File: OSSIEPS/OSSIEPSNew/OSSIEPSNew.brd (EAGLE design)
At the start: 94 x 88 mm, 99 parts, among them U1 LT3479, U11 SN74LVC1T45-EP, U13 MAX890L, U14 MAX890L, U2 MAX4376, U3 LT3652, U4 LTC4411, U5 LTC4411, U6 LTC4425, U8 LTC4411, X1 ESQ-126-38-G-D, X2 53015-03, X3 5268-02, X4 5268-02, X5 5268-03, X6 5268-02, X8 E62-10K

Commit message: eps board almost done
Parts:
- moved R17 3.01 mm to (17.8, 19.7), turned to 180 degrees
- moved R25 2.02 mm to (17.8, 16.7), turned to 0 degrees
- moved C6 1.27 mm to (24.4, 31.9)
- moved C1 1.27 mm to (16.2, 25.1)
- moved C2 1.27 mm to (21.0, 36.5)
- moved C5 1.27 mm to (25.4, 29.2)
- moved C7 1.27 mm to (25.6, 34.3)
- moved C8 1.27 mm to (23.2, 35.6)
- moved C9 1.27 mm to (21.9, 26.4)
- moved D1 1.27 mm to (16.2, 38.4)
- moved JP7 1.27 mm to (6.35, 44.1)
- moved L2 1.27 mm to (9.53, 34.3)
- moved R1 1.27 mm to (15.6, 27.0)
- moved R2 1.27 mm to (26.0, 31.3)
- moved R3 1.27 mm to (25.4, 27.6)
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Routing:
- net 3.3VOBC: track 5.14 -> 174.9 mm, vias 0 -> 4
- net VBUS: track 70.8 -> 230.2 mm, vias 2 -> 8
- net VSUPERCAP: track 51.7 -> 147.8 mm, vias 2 -> 4
- net SCCHG_EN: track 9.86 -> 105.1 mm, vias 0 -> 4
- net SCOUT_EN: track 13.2 -> 93.8 mm, vias 0 -> 4
- net SC_-PFO: track 10.7 -> 80.8 mm, vias 2 -> 4
- net SC_-ON: track 3.42 -> 70.8 mm, vias 0 -> 3
- net BAT_-CHRG: track 10.7 -> 77.3 mm, vias 0 -> 3
- net BAT_-FAULT: track 7.09 -> 72.8 mm, vias 0 -> 1
- net VBAT: track 125.8 -> 186.2 mm, vias 3 -> 5
- net SOLAR_-ON: track 33.1 -> 69.4 mm, vias 0 -> 2
- net VSC_IN: track 0.00 -> 20.5 mm
- net BAT_-ON: track 3.26 -> 20.8 mm
- net GND: track 32.8 -> 40.1 mm, vias 66 -> 70
- net N$46: track 68.7 -> 65.9 mm
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
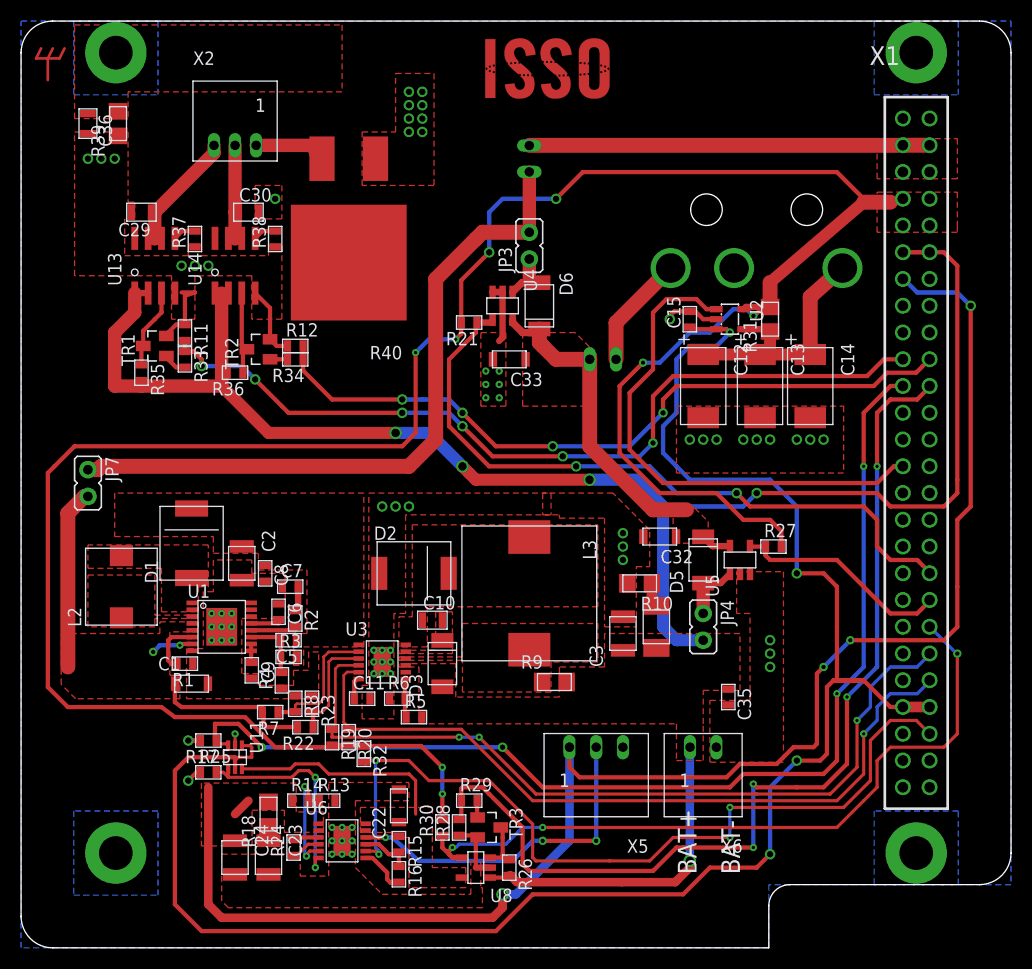
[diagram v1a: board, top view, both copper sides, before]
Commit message: battery supercap board added / library added
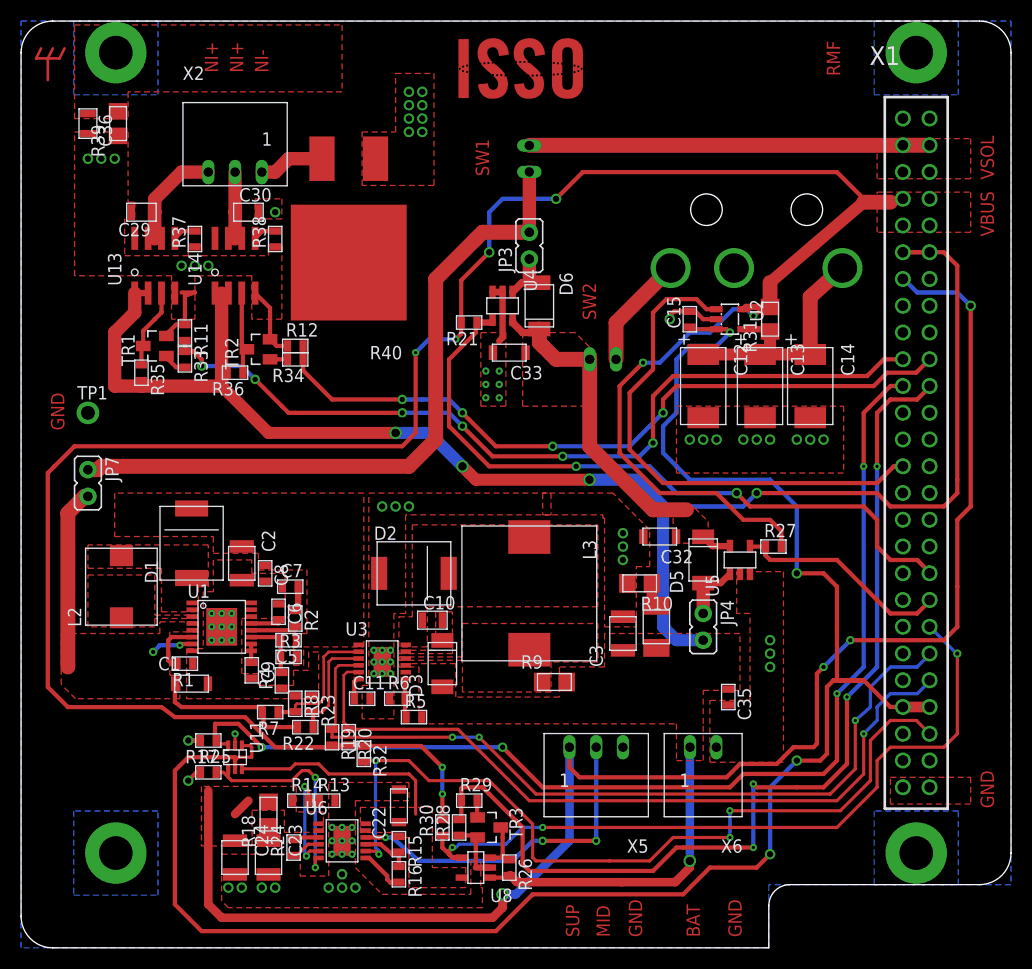
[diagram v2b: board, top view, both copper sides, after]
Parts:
- added TP1: TP, OSSI:TP-13
- X2: value 53015-03 -> 5268-03; device OSSI:53015-03 -> OSSI:5268-03
- moved X2 2.54 mm to (20.3, 73.7)
- moved U$1 2.54 mm to (53.3, 86.4)
- moved C33 0.63 mm to (46.4, 56.5)
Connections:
- net GND: now also TP1.TP
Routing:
- net ANT_COIL2: track 10.5 -> 7.99 mm
- net ANT_COIL1: track 13.3 -> 12.0 mm
- net N$57: track 7.15 -> 6.24 mm
- net N$20: track 20.8 -> 21.5 mm
- net GND: vias 70 -> 78
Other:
- board text added: "BAT"
- board text added: "GND"
- board text added: "MID"
- board text added: "NI+"
- board text added: "NI-"
- board text added: "RMF"
- board text added: "SUP"
- board text added: "SW1"
- board text added: "SW2"
- board text added: "VBUS"
- board text added: "VSOL"
- board text removed: "BAT+"
- board text removed: "BAT-"

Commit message: beta 1 release
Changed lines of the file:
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@@
 <setting verticaltext="up"/>
 </settings>
-<grid distance="1" unitdist="mm" unit="mm" style="lines" multiple="1" display="yes" altdistance="0.0125" altunitdist="inch" altunit="inch"/>
+<grid distance="1.27" unitdist="mm" unit="mm" style="lines" multiple="1" display="yes" altdistance="0.0125" altunitdist="inch" altunit="inch"/>
 <layers>
 <layer number="1" name="Top" color="4" fill="1" visible="yes" active="yes"/>
@@
 <layer number="27" name="tValues" color="7" fill="1" visible="no" active="yes"/>
 <layer number="28" name="bValues" color="7" fill="1" visible="no" active="yes"/>
-<layer number="29" name="tStop" color="7" fill="3" visible="no" active="yes"/>
+<layer number="29" name="tStop" color="7" fill="3" visible="yes" active="yes"/>
 <layer number="30" name="bStop" color="7" fill="6" visible="no" active="yes"/>
 <layer number="31" name="tCream" color="7" fill="4" visible="no" active="yes"/>
@@
 <text x="54.5934875" y="59.608721875" size="1.27" layer="29" font="vector" rot="SR90">SW2</text>
 <text x="44.4334875" y="73.261221875" size="1.27" layer="29" font="vector" rot="SR90">SW1</text>
-<text x="92.3759875" y="72.943721875" size="1.27" layer="1" font="vector" rot="SR90">VSOL</text>
-<text x="92.3759875" y="67.546221875" size="1.27" layer="1" font="vector" rot="SR90">VBUS</text>
-<text x="92.3759875" y="67.546221875" size="1.27" layer="29" font="vector" rot="SR90">VBUS</text>
-<text x="92.3759875" y="72.943721875" size="1.27" layer="29" font="vector" rot="SR90">VSOL</text>
-<text x="92.3759875" y="13.253721875" size="1.27" layer="1" font="vector" rot="SR90">GND</text>
-<text x="92.3759875" y="13.253721875" size="1.27" layer="29" font="vector" rot="SR90">GND</text>
+<text x="92.3759875" y="78.341221875" size="1.27" layer="1" font="vector" rot="SR90">VSOL</text>
+<text x="92.3759875" y="62.466221875" size="1.27" layer="1" font="vector" rot="SR90">VBUS</text>
+<text x="92.3759875" y="62.466221875" size="1.27" layer="29" font="vector" rot="SR90">VBUS</text>
+<text x="92.3759875" y="78.341221875" size="1.27" layer="29" font="vector" rot="SR90">VSOL</text>
+<text x="92.3759875" y="18.333721875" size="1.27" layer="1" font="vector" rot="SR90">GND</text>
+<text x="92.3759875" y="18.333721875" size="1.27" layer="29" font="vector" rot="SR90">GND</text>
 <text x="4.1109875" y="49.131221875" size="1.27" layer="29" font="vector" rot="SR90">GND</text>
 <text x="4.1109875" y="49.131221875" size="1.27" layer="1" font="vector" rot="SR90">GND</text>
@@
 <polygon width="0.3048" layer="1" thermals="no">
 <vertex x="82.55" y="16.1925"/>
-<vertex x="90.17" y="16.1925"/>
-<vertex x="90.17" y="13.6525"/>
+<vertex x="92.71" y="16.1925"/>
+<vertex x="92.71" y="13.6525"/>
 <vertex x="82.55" y="13.6525"/>
 </polygon>
@@
 <polygon width="0.3048" layer="1" thermals="no">
 <vertex x="81.28" y="71.755"/>
-<vertex x="90.17" y="71.755"/>
-<vertex x="90.17" y="67.945"/>
+<vertex x="92.71" y="71.755"/>
+<vertex x="92.71" y="67.945"/>
 <vertex x="81.28" y="67.945"/>
 </polygon>
@@
 <polygon width="0.3048" layer="1" thermals="no">
 <vertex x="81.28" y="76.835"/>
-<vertex x="90.17" y="76.835"/>
-<vertex x="90.17" y="73.025"/>
+<vertex x="92.71" y="76.835"/>
+<vertex x="92.71" y="73.025"/>
 <vertex x="81.28" y="73.025"/>
 </polygon>

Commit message: schematics renumbered
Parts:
- removed C29, C30: 100nF, 0805, OSSI:C0805(2012)
- removed C32, C33: 4.7uF, 1206, OSSI:C1206-GCM31
- removed C35: (no value), OSSI:C0603(1608)
- removed C36: (no value), OSSI:C0805(2012)
- removed D6: PMEG6020EP, OSSI:PMEG6020EP
- removed L3: 10uH, OSSI:RLF12545
- removed U11: SN74LVC1T45-EP, OSSI:SOT-6DCK
- removed U13, U14: MAX890L, OSSI:SO8
- removed X8: E62-10K, OSSI:E62-10K
- added C16: 100uF, OSSI:C1210-TMK325
- added C17, C21: 10uF, OSSI:C1210-GCM32
- added C18: 10nF, OSSI:C0603(1608)
- added C19: 470pF, OSSI:C0603(1608)
- added C20: 0.1uF, OSSI:C0603(1608)
- added D4: PMEG6020EP, OSSI:PMEG6020EP
- added L1: 4.7uH, OSSI:RLF7030
- added U10, U7: LTC4411, OSSI:TSOT23-5
- added U9: MAX4376, OSSI:SOT23-5DBV
- added X7: 5268-02, OSSI:5628-02
- C1: value 2.2uF -> (none); device OSSI:C1206-GCM31 -> OSSI:C0805(2012)
- C10: value 1uF, 100V -> 0 Ohm; device OSSI:C0805(2012) -> OSSI:C0603(1608)
- C11: value 0 Ohm -> (none)
- C2, C3: value 10uF -> 100nF, 0805; device OSSI:C1210-GCM32 -> OSSI:C0805(2012)
- C22: value 2.2uF -> 1uF, 100V; device OSSI:C1206-GCM31 -> OSSI:C0805(2012)
- C23: value 22uF -> 0.1uF; device OSSI:C1210-GCM32 -> OSSI:C0603(1608)
- C24: value 22uF -> 4.7uF, 1206; device OSSI:C1210-GCM32 -> OSSI:C1206-GCM31
- C4: value 100uF -> 2.2uF; device OSSI:C1210-TMK325 -> OSSI:C1206-GCM31
- C5: value 470pF -> 22uF; device OSSI:C0603(1608) -> OSSI:C1210-GCM32
- C6: value 0.1uF -> 22uF; device OSSI:C0603(1608) -> OSSI:C1210-GCM32
- C7: value 10nF -> 100pF
- C8: value 0.1uF -> 2.2uF; device OSSI:C0603(1608) -> OSSI:C1206-GCM31
- C9: value 100pF -> 4.7uF, 1206; device OSSI:C0603(1608) -> OSSI:C1206-GCM31
- D1: value STPS5L60 -> PMEG6020EP; device OSSI:STPS5L60 -> OSSI:PMEG6020EP
- D3: value PMEG6020EP -> STPS5L60; device OSSI:PMEG6020EP -> OSSI:STPS5L60
- L2: value 4.7uH -> 10uH; device OSSI:RLF7030 -> OSSI:RLF12545
- R1: value 17.8k -> 511; device OSSI:R0603(1608) -> OSSI:WSL1206
- R10: value 0.1 -> 100k; device OSSI:WSL1206 -> OSSI:R0603(1608)
- R12: value 47k -> 1.5k
- R13: value 750k -> 470k
- R14: value 1.5M -> 511; device OSSI:R0603(1608) -> OSSI:WSL1206
- R15: value 1.5M -> 470k
- R17, R20, R30: value 470k -> 1.5M
- R18: value 511 -> 2k; device OSSI:WSL1206 -> OSSI:R0603(1608)
- R2: value 4.3k -> 47k
- R21: value 470k -> 750k
- R22: value 200k -> 470k
- R23: value 100k -> 470k
- R24: value 2k -> 17.8k
- R25: value 470k -> 30.9k
- R26: value 470k -> 0.1; device OSSI:R0603(1608) -> OSSI:WSL1206
- R27: value 470k -> 169k
- R28: value 47k -> 100k
- R29: value 1.5k -> 100k
- R3: value 169k -> 1.5k
- R31: value 20m / 10m -> 4.3k; device OSSI:WSL1206 -> OSSI:R0603(1608)
- R32: value 470k -> 300k
- R33: value 1.5k -> 200k
- R34: value 1.5k -> 36k
- R35: value 100k -> 20m / 10m; device OSSI:R0603(1608) -> OSSI:WSL1206
- R36: value 100k -> 0.05; device OSSI:R0603(1608) -> OSSI:WSL1206
- R37, R38: value 1.2k -> 470k
- R39: value 511 -> 470k; device OSSI:WSL1206 -> OSSI:R0603(1608)
- R4: value 30.9k -> 1.2k
- R40: value 1R5, 20W, 1% -> 470k; device OSSI:PWR263S-20 -> OSSI:R0603(1608)
- R5: value 300k -> 1R5, 20W, 1%; device OSSI:R0603(1608) -> OSSI:PWR263S-20
- R6: value 1.5M -> 47k
- R7: value 36k -> 1.2k
- R8: value 100k -> 1.5k
- R9: value 0.05 -> 100k; device OSSI:WSL1206 -> OSSI:R0603(1608)
- U1: value LT3479 -> MAX890L; device OSSI:TSSOP16-FE -> OSSI:SO8
- U2: value MAX4376 -> MAX890L; device OSSI:SOT23-5DBV -> OSSI:SO8
- U3: value LT3652 -> LTC4411; device OSSI:MSE -> OSSI:TSOT23-5
- U4: value LTC4411 -> LTC4425; device OSSI:TSOT23-5 -> OSSI:MSE
- U5: value LTC4411 -> SN74LVC1T45-EP; device OSSI:TSOT23-5 -> OSSI:SOT-6DCK
- U6: value LTC4425 -> LT3479; device OSSI:MSE -> OSSI:TSSOP16-FE
- U8: value LTC4411 -> LT3652; device OSSI:TSOT23-5 -> OSSI:MSE
- X3: value 5268-02 -> 5268-03; device OSSI:5628-02 -> OSSI:5268-03
- X5: value 5268-03 -> 5268-02; device OSSI:5268-03 -> OSSI:5628-02
- X6: value 5268-02 -> E62-10K; device OSSI:5628-02 -> OSSI:E62-10K
- moved H1 76.0 mm to (9.00, 9.00)
- moved H2 76.0 mm to (85.0, 9.00)
- moved H3 76.0 mm to (85.0, 85.0)
- moved H4 76.0 mm to (9.00, 85.0)
- moved C23 64.9 mm to (63.5, 59.7), turned to 90 degrees
- moved R37 62.2 mm to (71.4, 38.1), turned to 0 degrees
- moved R39 61.7 mm to (29.5, 20.0), turned to 270 degrees
- moved C3 60.8 mm to (11.4, 69.8), turned to 180 degrees
- moved R35 59.9 mm to (71.1, 59.7), turned to 90 degrees
- moved X4 58.3 mm to (64.8, 19.1), flipped to the top, turned to 180 degrees
- moved U2 54.8 mm to (12.7, 64.8), turned to 0 degrees
- moved C24 54.6 mm to (46.4, 56.5), turned to 180 degrees
- moved C1 54.1 mm to (6.35, 78.3), turned to 270 degrees
- moved R11 53.7 mm to (41.6, 11.4), turned to 90 degrees
- moved R5 53.4 mm to (31.1, 74.9), turned to 180 degrees
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- renumbered JP4 to JP1, JP7 to JP2
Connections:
- net 3.3VOBC: now also C23.1, U5.1, U5.5, U9.3; no longer C15.1, U11.1, U11.5, U2.3
- net ANT_COIL1: now also C3.1, U2.6, U2.7; no longer C29.1, U13.6, U13.7
- net ANT_COIL2: now also C2.1, U1.6, U1.7; no longer C30.1, U14.6, U14.7
- net ANT_DEPLOY1: now also R6.2, R8.1; no longer R11.2, R33.1
- net ANT_DEPLOY2: now also R2.2, R3.1; no longer R12.2, R34.1
- net BAT_-CHRG: now also R39.1, U8.4; no longer R19.1, U3.4
- net BAT_-FAULT: now also R38.1, U8.5; no longer R20.1, U3.5
- net BAT_-ON: now also R37.1, U7.P$4; no longer R27.1, U5.P$4
- net BUS_CS: now also U9.1; no longer U2.1
- net GND: now also C1.2, C10.2, C15.1, C17.P$2, C18.1, C2.2, C20.2, C21.P$2, C23.2, C3.2, C4.P$2, C5.P$2, C6.P$2, C7.2, C8.P$2, C9.P$2, D3.A, R1.P$1, R16.2, R18.1, R2.1, R22.1, R23.2, R26.P$2, R29.1, R30.1, R5.P$1, R7.1, U1.4, U10.P$2, U10.P$3, U2.4, U3.P$2, U4.13, U4.4, U5.2, U6.14, U6.15, U6.16, U6.8, U6.PPAD, U7.P$2, U7.P$3, U8.13, U9.2, X3.3, X4.2; no longer C1.P$2, C15.2, C2.P$2, C22.P$2, C23.P$2, C29.2, C3.P$2, C30.2, C32.P$2, C33.P$2, C35.2, C36.2, C6.1, C7.1, C8.2, C9.2, D2.A, R1.1, R10.P$2, R12.1, R13.2, R17.2, R23.1, R37.1, R38.1, R39.P$1, R40.P$1, R8.1, U1.14, U1.15, U1.16, U1.8, U1.PPAD, U11.2, U13.4, U14.4, U2.2, U3.13, U4.P$2, U4.P$3, U5.P$2, U5.P$3, U6.13, U6.4, U8.P$2, X5.3, X6.2
- net N$1: now also L1.P$1, U6.3; no longer L2.P$1, U1.3
- net N$10: now also C7.1, U6.10, U6.9; no longer C9.1, U1.10, U1.9
- net N$11: now also R24.2, U6.6; no longer R1.2, U1.6
- net N$12: now also R28.2, R33.1, U8.3; no longer R22.1, R23.2, U3.3
- net N$13: now also C22.2, D1.C, U8.11; no longer C10.2, D3.C, U3.11
- net N$14: now also R16.1, R20.2, U4.5; no longer R13.1, R14.2, U6.5
- net N$16: now also C22.1, D3.C, L2.P$1, U8.12; no longer C10.1, D2.C, L3.P$1, U3.12
- net N$17: now also R30.2, R32.1, U8.7; no longer R5.1, R6.2, U3.7
- net N$18: now also C24.P$1, C9.P$1, D4.C, U10.P$5, U7.P$5, X5.2; no longer C32.P$1, C33.P$1, D6.C, U4.P$5, U5.P$5, X3.2
- net N$19: now also C10.1, U8.6; no longer C11.1, U3.6
- net N$2: now also R29.2, R34.1, U8.2; no longer R7.1, R8.2, U3.2
- net N$20: now also R22.2, U4.6, U5.4; no longer R25.2, U11.4, U6.6
- net N$21: now also C5.P$1, R14.P$1; no longer C23.P$1, R18.P$1
- net N$22: now also R13.1, U3.P$3; no longer R26.1, U8.P$3
- net N$23: now also R12.2; no longer R29.2
- net N$24: now also R35.P$1, U9.4, X6.C; no longer R31.P$1, U2.4, X8.C
- net N$29: now also R17.2, R21.1, U4.9; no longer R15.2, R16.1, U6.9
- net N$3: now also C19.1, C20.1, C21.P$1, D2.C, R27.2, U8.1; no longer C2.P$1, C5.1, C8.1, D1.C, R3.2, U3.1
- net N$31: now also R21.2, U4.7; no longer R16.2, U6.7
- net N$33: now also R3.2, TR1.1; no longer R34.2, TR2.1
- net N$37: now also U2.8; no longer U13.8
- net N$38: now also U1.8; no longer U14.8
- net N$39: now also D5.A, U10.P$1; no longer D6.A, U4.P$1
- net N$4: now also C16.P$2, R26.P$1; no longer C4.P$2, R10.P$1
- net N$40: now also R18.2, U4.3; no longer R24.2, U6.3
- net N$42: now also D4.A, U7.P$1; no longer D5.A, U5.P$1
- net N$44: now also C8.P$1, R33.2, R34.2, U6.4, U6.5, U6.7; no longer C1.P$1, R22.2, R7.2, U1.4, U1.5, U1.7
- net N$46: now also X7.1; no longer X4.1
- net N$49: now also R8.2, TR2.1; no longer R33.2, TR1.1
- net N$5: now also C15.2, U6.13; no longer C6.2, U1.13
- net N$50: now also R9.1, TR2.3, U2.3; no longer R35.1, TR1.3, U13.3
- net N$51: now also R10.1, TR1.3, U1.3; no longer R36.1, TR2.3, U14.3
- net N$52: now also R7.2, U2.5; no longer R37.2, U13.5
- net N$53: now also R4.2, U1.5; no longer R38.2, U14.5
- net N$54: now also X5.1, X6.NC; no longer X3.1, X8.NC
- net N$57: now also R5.P$2; no longer R40.P$2
- net N$6: now also D2.A, L1.P$2, U6.1, U6.2; no longer D1.A, L2.P$2, U1.1, U1.2
- net N$7: now also C18.2, R31.1; no longer C7.2, R2.1
- net N$8: now also R31.2, U6.12; no longer R2.2, U1.12
- net N$9: now also C19.2, R25.2, R27.1, U6.11; no longer C5.2, R3.1, R4.2, U1.11
- net SCCHG_EN: now also R23.1, U5.3; no longer R17.1, U11.3
- net SCOUT_EN: now also R11.2, R12.1; no longer R28.2, R29.1
- net SC_-ON: now also R15.1, U3.P$4; no longer R30.1, U8.P$4
- net SC_-PFO: now also R19.2, U4.8; no longer R32.2, U6.8
- net SENSE: now also L2.P$2, R36.P$1, U8.10; no longer L3.P$2, R9.P$1, U3.10
- net SOLAR_-ON: now also R40.1, U10.P$4; no longer R21.1, U4.P$4
- net STRUT_GND: now also C1.1, H4.B3,2, R1.P$2; no longer C36.1, H1.B3,2, R39.P$2
- net VBAT: now also C11.1, C16.P$1, C17.P$1, D1.A, R10.2, R13.2, R32.2, R36.P$2, R9.2, U1.1, U1.2, U2.1, U2.2, U3.P$1, U8.9, X4.1; no longer C3.P$1, C35.1, C4.P$1, D3.A, R26.2, R35.2, R36.2, R5.2, R9.P$2, U13.1, U13.2, U14.1, U14.2, U3.9, U8.P$1, X6.1
- net VBUS: now also R15.2, R19.1, R35.P$2, R37.2, R38.2, R39.2, R40.2, U9.5; no longer R19.2, R20.2, R21.2, R27.2, R30.2, R31.P$2, R32.1, U2.5
- net VMID: now also U4.10, X3.2; no longer U6.10, X5.2
- net VSC_IN: now also C4.P$1, R17.1, U3.P$5, U4.11, U4.12, U5.6; no longer C22.P$1, R15.1, U11.6, U6.11, U6.12, U8.P$5
- net VSOLAR: now also X7.2; no longer X4.2
- net VSUPERCAP: now also C6.P$1, R14.P$2, R20.1, U4.1, U4.2, X3.1; no longer C24.P$1, R14.1, R18.P$2, U6.1, U6.2, X5.1
